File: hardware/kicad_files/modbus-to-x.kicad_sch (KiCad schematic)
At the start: 40 parts, among them IC1 ESP32-WROOM-32D_M113DH2800PH3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, J1 615006138421, J4 M50-3140545R, Q1 DSS4160U-7, Q2 DSS4160U-7, SW1 SW_Wuerth_450301014042, SW4 3983, U1 LM2596S-3.3, U3 MAX3485

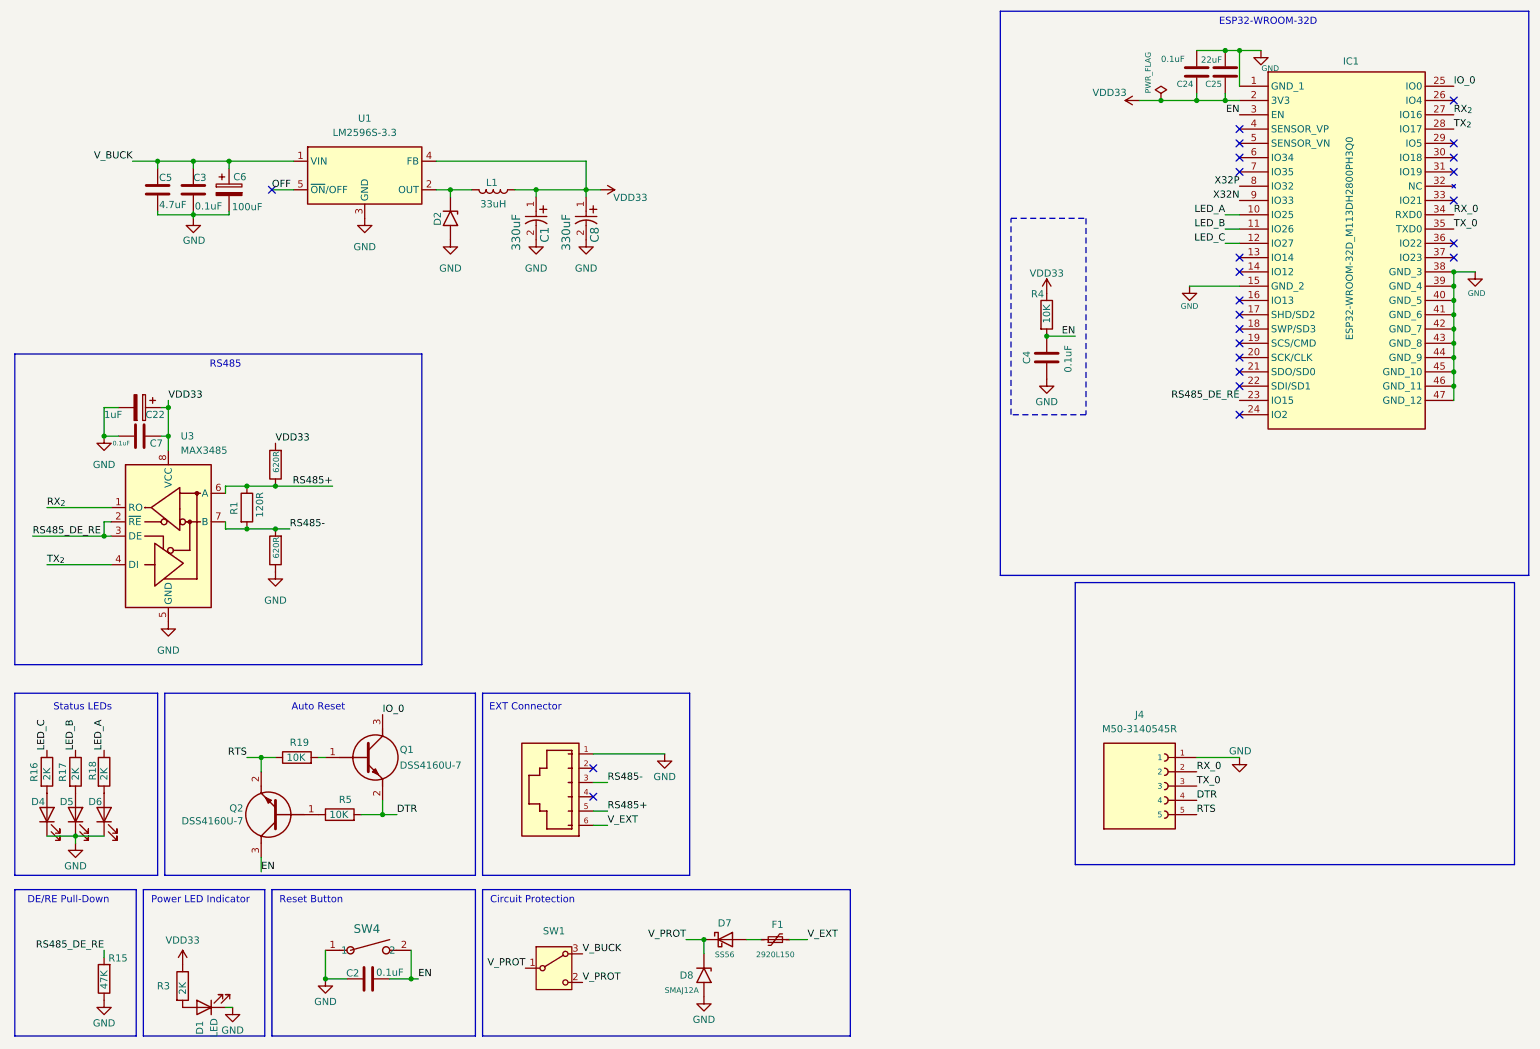
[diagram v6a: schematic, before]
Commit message: small trace refinements
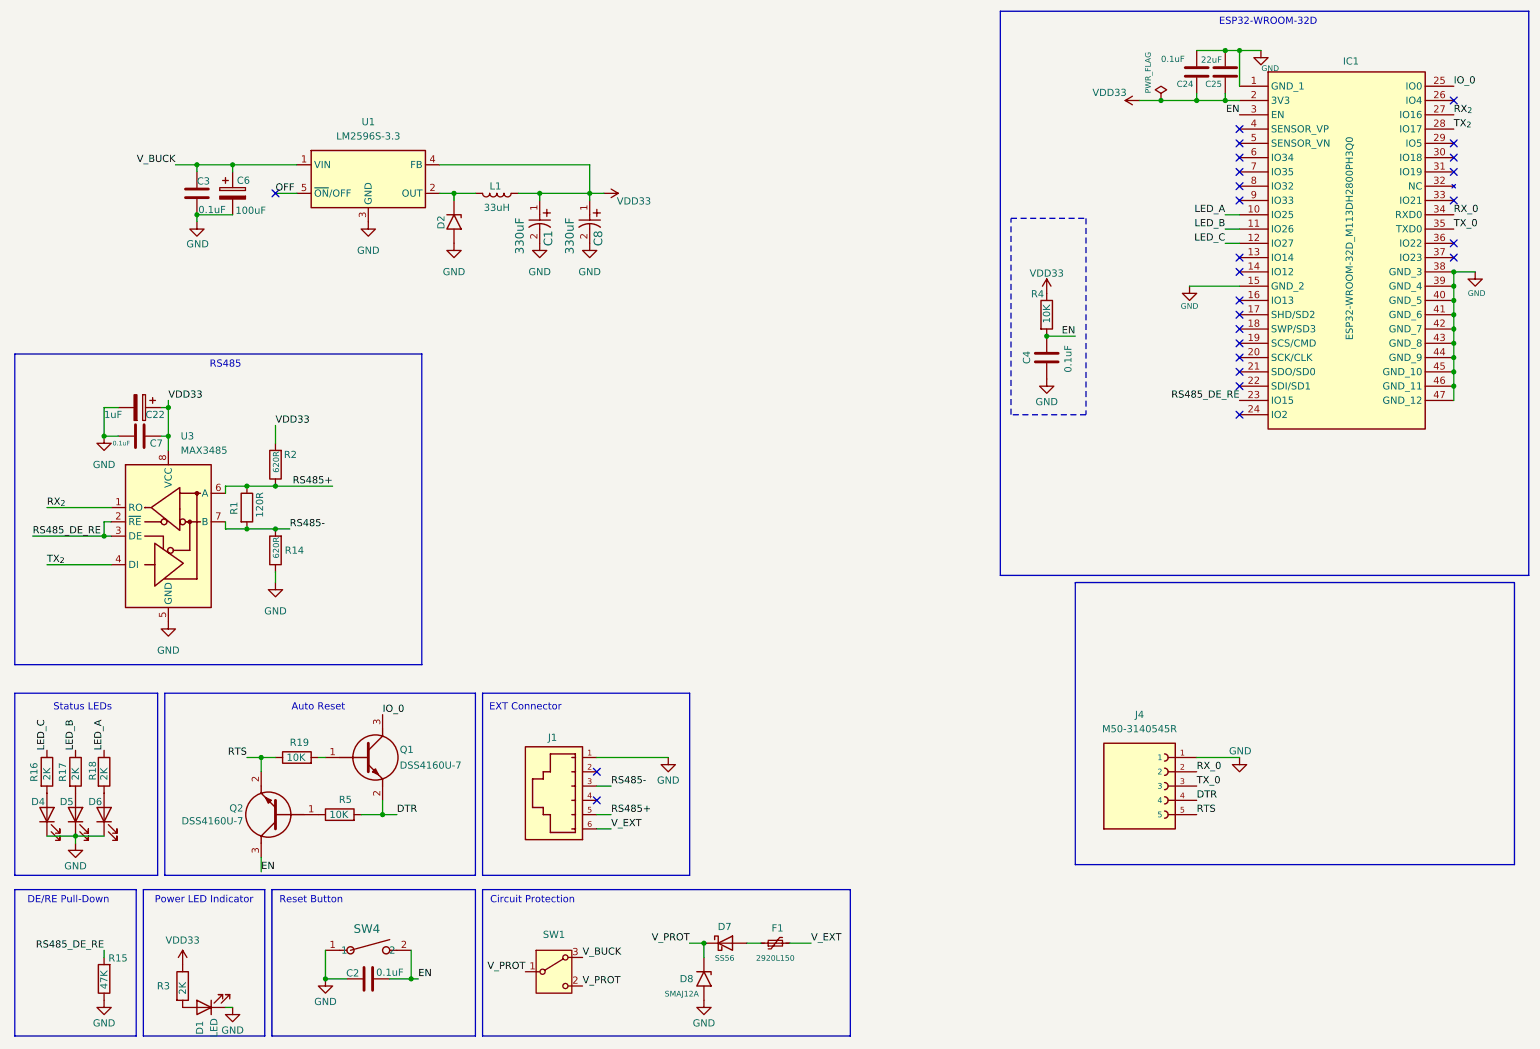
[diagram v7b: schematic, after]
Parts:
- removed C5: 4.7uF, Capacitor_SMD:C_0805_2012Metric, symbol Device:C
- C3: footprint Capacitor_SMD:C_0805_2012Metric -> Capacitor_SMD:C_0603_1608Metric; Id C #43 -> C #TBD; PartNo 08055C104KAT2A -> C0603C104K5RACTU; Voltage (none) -> 50V
- C4: footprint Capacitor_SMD:C_1206_3216Metric_Pad1.33x1.80mm_HandSolder -> Capacitor_SMD:C_0805_2012Metric
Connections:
- net X32N: no longer names the net of IC1.9 (IO33)
- net X32P: no longer names the net of IC1.8 (IO32)
- no-connect marks 24 -> 26
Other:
- moved on the sheet: C1, C3, C6, C8, D2, D7, D8, F1, L1, SW1, U1
